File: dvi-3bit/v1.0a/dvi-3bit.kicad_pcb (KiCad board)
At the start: 4 copper layers, 37 x 20.3 mm, 32 parts, among them J1 PMOD, J2 jmp, J3 5V, J4 jmp, J5 HDMI_A_1.4, U1 VREG_3V3, U2 TFP410

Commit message: Renamed hdmi to dvi.
I am being told that using hdmi term has some legal implications so we
can't use it. *sigh*
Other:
- board text added: "iCEBreaker PMOD 3bit DVI"
- board text removed: "iCEBreaker PMOD 3bit HDMI"
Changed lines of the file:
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@@
   (page A4)
   (title_block
-    (title "iCEBreaker PMOD - Tristate LED")
+    (title "iCEBreaker PMOD - 3bit DVI")
     (rev V1.0a)
     (company 1BitSquared)
@@
     (effects (font (size 1.5 1.5) (thickness 0.3)) (justify mirror))
   )
-  (gr_text "iCEBreaker PMOD\n3bit HDMI" (at 60.85 40.1 270) (layer B.SilkS)
+  (gr_text "iCEBreaker PMOD\n3bit DVI" (at 60.85 40.1 270) (layer B.SilkS)
     (effects (font (size 1.5 1.5) (thickness 0.3)) (justify mirror))
   )

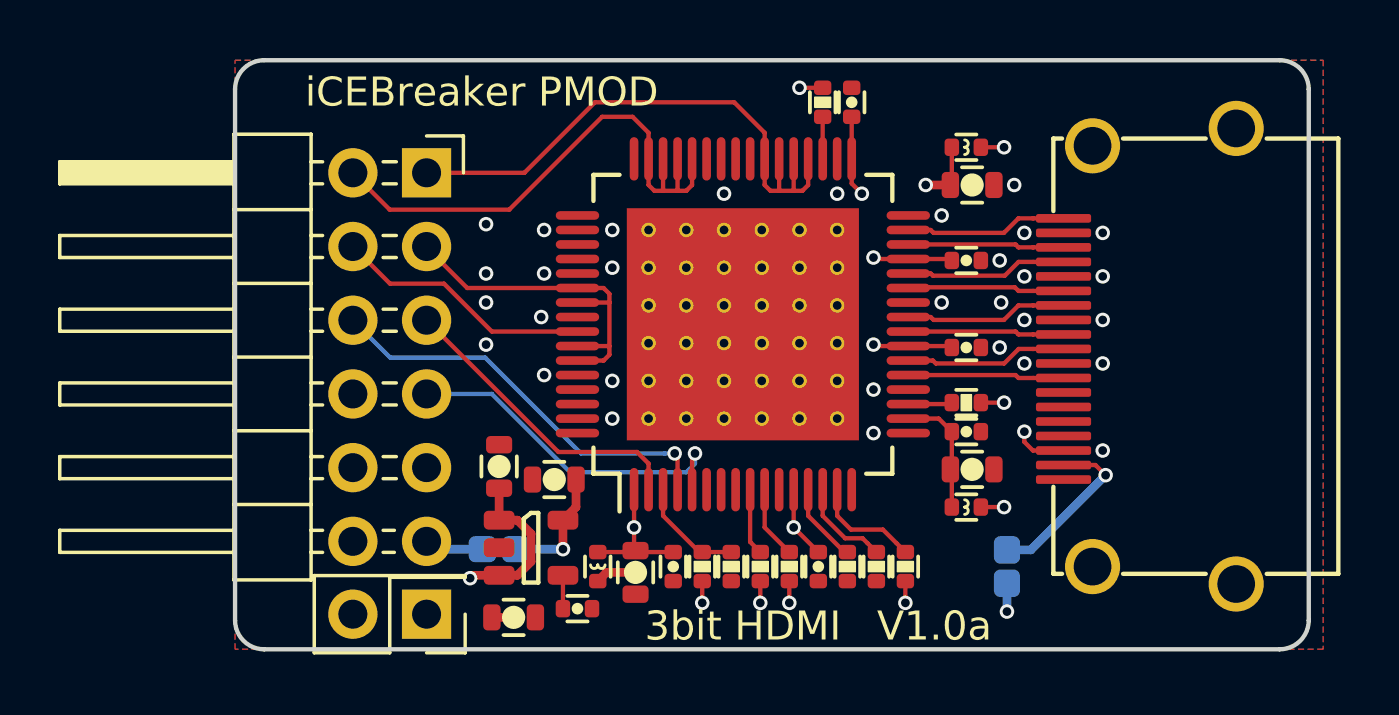
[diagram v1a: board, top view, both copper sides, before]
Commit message: Corrected pinout and added legend.
I made a mistake copying the pinout of the original @blackmesalabs
design. I mirroed it and now it should be correct. I also added
silkscreen legend of the pin signals.
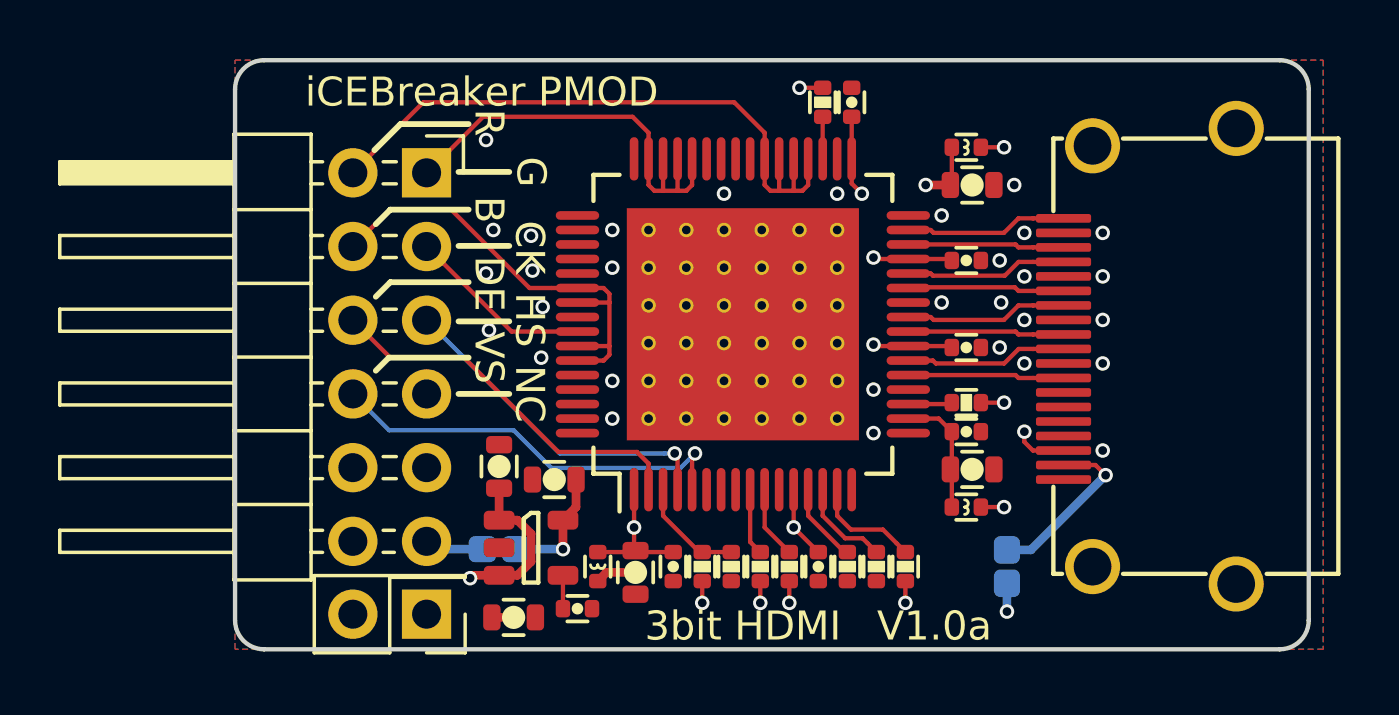
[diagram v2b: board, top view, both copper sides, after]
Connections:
- J1 pad 1: /RED -> /GRN
- J1 pad 10: Net-(J1-Pad10) -> /VS
- J1 pad 2: /BLU -> /CLK
- J1 pad 3: /DE -> /HS
- J1 pad 4: /VS -> Net-(J1-Pad4)
- J1 pad 7: /GRN -> /RED
- J1 pad 8: /CLK -> /BLU
- J1 pad 9: /HS -> /DE
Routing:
- net /GRN: track 18.8 -> 15.2 mm
- net /BLU: track 12.5 -> 16.1 mm
- net /DE: track 10.6 -> 13.1 mm
- net /RED: track 19.7 -> 22.2 mm
- net /HS: track 14.3 -> 11.7 mm
- net /CLK: track 8.95 -> 6.44 mm
- net /VS: track 12.1 -> 14.3 mm
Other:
- board text added: "B"
- board text added: "CK"
- board text added: "DE"
- board text added: "G"
- board text added: "HS"
- board text added: "NC"
- board text added: "R"
- board text added: "VS"

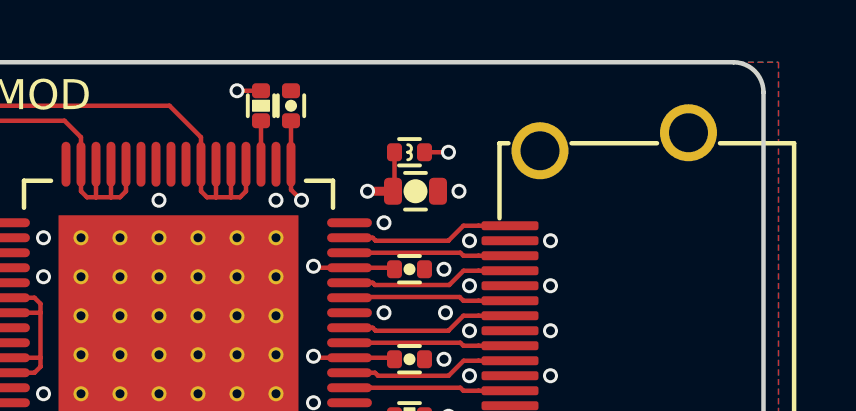
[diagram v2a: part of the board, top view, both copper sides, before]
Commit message: Added 3d model for the HDMI connector.
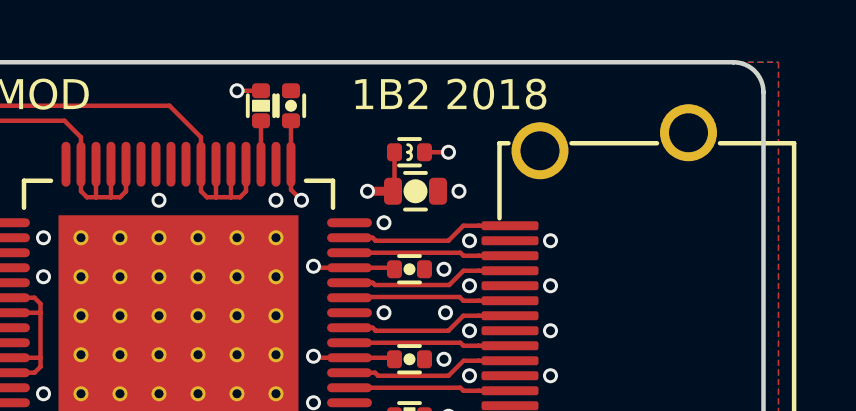
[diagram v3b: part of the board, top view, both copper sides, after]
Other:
- board text added: "1B2 2018"
- board text added: "1BitSquared 2018"
- board text added: "CC-BY-SA"
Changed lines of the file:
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@@
   (general
     (thickness 1.6)
-    (drawings 54)
+    (drawings 57)
     (tracks 268)
     (zones 0)
@@
     (pad SH thru_hole circle (at -7.85 5 90) (size 1.9 1.9) (drill 1.3) (layers *.Cu *.Mask)
       (net 1 GND))
+    (model ${KIPRJMOD}/../../lib/pkl/packages3d/pkl_connectors.3dshapes/HDMI-10029449-111RLF.stp
+      (offset (xyz 0 -1.7 3.45))
+      (scale (xyz 1 1 1))
+      (rotate (xyz 180 0 0))
+    )
   )
   (module Connector_PinHeader_2.54mm:PinHeader_2x01_P2.54mm_Vertical (layer F.Cu)
@@
     )
   )
+  (gr_text "1BitSquared 2018" (at 55.35 40.2 270) (layer B.SilkS)
+    (effects (font (size 1 1) (thickness 0.2)) (justify mirror))
+  )
+  (gr_text CC-BY-SA (at 53.6 40.25 270) (layer B.SilkS)
+    (effects (font (size 1 1) (thickness 0.2)) (justify mirror))
+  )
+  (gr_text "1B2 2018" (at 56.55 31.1) (layer F.SilkS)
+    (effects (font (size 1 1) (thickness 0.2)))
+  )
   (gr_line (start 37.7 33.85) (end 39.45 33.85) (layer B.SilkS) (width 0.2))

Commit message: Some global cleanup.
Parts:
- added REF**: null_Logo_SilkS_7.5mm, pkl_logos:null_Logo_SilkS_7.5mm, B.Cu at (47.5, 40.2)
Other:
- board text added: "NULL"
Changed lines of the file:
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@@
-(kicad_pcb (version 20171130) (host pcbnew 5.0.0-fee4fd1~66~ubuntu18.04.1)
+(kicad_pcb (version 20171130) (host pcbnew 5.1.5-52549c5~86~ubuntu19.10.1)
   (general
     (thickness 1.6)
-    (drawings 57)
+    (drawings 58)
     (tracks 268)
     (zones 0)
-    (modules 32)
+    (modules 33)
     (nets 44)
   )
@@
     (zone_45_only no)
     (trace_min 0.15)
-    (segment_width 0.2)
-    (edge_width 0.15)
     (via_size 0.5)
     (via_drill 0.3)
@@
     (uvia_min_size 0.2)
     (uvia_min_drill 0.1)
+    (edge_width 0.15)
+    (segment_width 0.2)
     (pcb_text_width 0.3)
     (pcb_text_size 1.5 1.5)
@@
     (add_net "Net-(U2-Pad7)")
     (add_net "Net-(U2-Pad8)")
+  )
+  (module pkl_logos:null_Logo_SilkS_7.5mm (layer B.Cu)
+    (at 47.5 40.2 90)
+    (fp_text reference REF** (at 0 -4.55 90) (layer B.Fab)
+      (effects (font (size 1 1) (thickness 0.15)) (justify mirror))
+    )
+    (fp_text value null_Logo_SilkS_7.5mm (at 0 4.55 90) (layer B.Fab)
+      (effects (font (size 1 1) (thickness 0.15)) (justify mirror))
+    )
+    (fp_line (start 1 -0.5) (end 1.5 -0.5) (layer B.SilkS) (width 0.15))
+    (fp_line (start 1 0.5) (end 1 -0.5) (layer B.SilkS) (width 0.15))
+    (fp_line (start 0.2 -0.5) (end 0.7 -0.5) (layer B.SilkS) (width 0.15))
+    (fp_line (start 0.2 0.5) (end 0.2 -0.5) (layer B.SilkS) (width 0.15))
+    (fp_line (start -0.1 -0.2) (end -0.1 0.5) (layer B.SilkS) (width 0.15))
+    (fp_arc (start -0.4 -0.2) (end -0.7 -0.2) (angle 180) (layer B.SilkS) (width 0.15))
+    (fp_line (start -0.7 0.5) (end -0.7 -0.2) (layer B.SilkS) (width 0.15))
+    (fp_line (start -1 -0.5) (end -1 0.5) (layer B.SilkS) (width 0.15))
+    (fp_line (start -1.5 0.5) (end -1 -0.5) (layer B.SilkS) (width 0.15))
+    (fp_line (start -1.5 -0.5) (end -1.5 0.5) (layer B.SilkS) (width 0.15))
+    (fp_line (start 3.75 3.75) (end -3.75 3.75) (layer B.SilkS) (width 0.3))
+    (fp_line (start -3.75 3.75) (end -3.75 -3.75) (layer B.SilkS) (width 0.3))
+    (fp_line (start 3.75 3.75) (end 3.75 -3.75) (layer B.SilkS) (width 0.3))
+    (fp_line (start -3.75 -3.75) (end 3.75 -3.75) (layer B.SilkS) (width 0.3))
   )
   (module pkl_housings_qfp:TQFP-64-1EP_10x10mm_P0.5mm_EP5x5mm (layer F.Cu)
@@
     )
   )
+  (gr_text NULL (at 42.3 40.2 270) (layer B.SilkS)
+    (effects (font (size 1 1) (thickness 0.2)) (justify mirror))
+  )
   (gr_text "1BitSquared 2018" (at 55.35 40.2 270) (layer B.SilkS)
